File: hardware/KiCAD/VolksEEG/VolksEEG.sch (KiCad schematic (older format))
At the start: 0 parts

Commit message: Added more tasks following re-watch of 1st half of previous design review.
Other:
- note added: "Known Remaining Tasks:\n* Finish Referential Montage configuration of ADS1299 Electrodes.\n* Add Debugging bits, Test points, 0Ohm Links, indicator LEDs? \n* Double Check ADS1299 Connections.\n* Add component values.\n* Adjust names of hierarchical pins to sheets.\n* Seperate Analogue and digital supplies?\n* Check SD Card connections.\n* Decoupling caps.\n* Check Power up sequencing."
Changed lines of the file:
@@
 Title "Main"
 Date ""
-Rev "6378737"
+Rev ""
 Comp "VolksEEG"
 Comment1 ""
@@
 $EndDescr
 $Sheet
-S 6600 3000 1050 2350
+S 6600 1750 1050 2350
 U 615BA110
 F0 "ADS1299" 50
 F1 "ADS1299.sch" 50
-F2 "nCS_ads" I L 6600 3800 50
-F3 "SCK_ads" I L 6600 3950 50
-F4 "MOSI_ads" I L 6600 3500 50
-F5 "MISO_ads" O L 6600 4100 50
-F6 "nRST_ads" I L 6600 3650 50
-F7 "AIN5" I R 7650 4100 50
-F8 "AIN6" I R 7650 4250 50
-F9 "AIN7" I R 7650 4400 50
-F10 "AIN8" I R 7650 4550 50
-F11 "AIN1" I R 7650 3500 50
-F12 "AIN2" I R 7650 3650 50
-F13 "AIN3" I R 7650 3800 50
-F14 "AIN4" I R 7650 3950 50
-F15 "ADS_nDRDY_ads" O L 6600 4250 50
-F16 "+3V3_ads" I L 6600 4500 50
-F17 "+2V5_ads" I L 6600 4650 50
-F18 "-2V5_ads" I L 6600 4800 50
-F19 "GND_ads" I L 6600 4950 50
-F20 "REF" I R 7650 4800 50
-F21 "BIAS_OUT" O R 7650 4950 50
-F22 "BIAS_INV" O R 7650 5100 50
+F2 "nCS_ads" I L 6600 2550 50
+F3 "SCK_ads" I L 6600 2700 50
+F4 "MOSI_ads" I L 6600 2250 50
+F5 "MISO_ads" O L 6600 2850 50
+F6 "nRST_ads" I L 6600 2400 50
+F7 "AIN5" I R 7650 2850 50
+F8 "AIN6" I R 7650 3000 50
+F9 "AIN7" I R 7650 3150 50
+F10 "AIN8" I R 7650 3300 50
+F11 "AIN1" I R 7650 2250 50
+F12 "AIN2" I R 7650 2400 50
+F13 "AIN3" I R 7650 2550 50
+F14 "AIN4" I R 7650 2700 50
+F15 "ADS_nDRDY_ads" O L 6600 3000 50
+F16 "+3V3_ads" I L 6600 3250 50
+F17 "+2V5_ads" I L 6600 3400 50
+F18 "-2V5_ads" I L 6600 3550 50
+F19 "GND_ads" I L 6600 3700 50
+F20 "REF" I R 7650 3550 50
+F21 "BIAS_OUT" O R 7650 3700 50
+F22 "BIAS_INV" O R 7650 3850 50
 $EndSheet
 $Sheet
-S 5250 4350 1000 1000
+S 5250 3100 1000 1000
 U 615BA255
 F0 "ADS1299 Power" 50
 F1 "Power.sch" 50
-F2 "GND_in" I L 5250 4650 50
-F3 "+3V3_out" O R 6250 4500 50
-F4 "+2V5_out" O R 6250 4650 50
-F5 "-2V5_out" O R 6250 4800 50
-F6 "+5V_in" I L 5250 4500 50
+F2 "GND_in" I L 5250 3400 50
+F3 "+3V3_out" O R 6250 3250 50
+F4 "+2V5_out" O R 6250 3400 50
+F5 "-2V5_out" O R 6250 3550 50
+F6 "+5V_in" I L 5250 3250 50
 $EndSheet
 $Sheet
-S 1500 3200 1200 1400
+S 1500 1950 1200 1400
 U 615BA20B
 F0 "nRF52840 Feather Sense Express Board" 50
 F1 "nRF52840.sch" 50
-F2 "MOSI_nrf" O R 2700 3500 50
-F3 "SCK_nrf" O R 2700 3950 50
-F4 "MISO_nrf" I R 2700 4100 50
-F5 "ADS-nRST_nrf" O R 2700 3650 50
-F6 "ADS-nCS_nrf" O R 2700 3800 50
-F7 "ADS-nDRDY_nrf" I R 2700 4250 50
-F8 "+3V3_nrf" O R 2700 3350 50
-F9 "GND_nrf" O R 2700 4400 50
+F2 "MOSI_nrf" O R 2700 2250 50
+F3 "SCK_nrf" O R 2700 2700 50
+F4 "MISO_nrf" I R 2700 2850 50
+F5 "ADS-nRST_nrf" O R 2700 2400 50
+F6 "ADS-nCS_nrf" O R 2700 2550 50
+F7 "ADS-nDRDY_nrf" I R 2700 3000 50
+F8 "+3V3_nrf" O R 2700 2100 50
+F9 "GND_nrf" O R 2700 3150 50
 $EndSheet
 Wire Wire Line
-	2700 3500 3450 3500
+	2700 2250 3450 2250
 Wire Wire Line
-	3450 3650 2700 3650
+	3450 2400 2700 2400
 Wire Wire Line
-	2700 3800 3450 3800
+	2700 2550 3450 2550
 Wire Wire Line
-	3450 3950 2700 3950
+	3450 2700 2700 2700
 Wire Wire Line
-	2700 4100 3450 4100
+	2700 2850 3450 2850
 Wire Wire Line
-	8150 4100 7650 4100
+	8150 2850 7650 2850
 Wire Wire Line
-	4800 3500 6600 3500
+	4800 2250 6600 2250
 Wire Wire Line
-	4800 3650 6600 3650
+	4800 2400 6600 2400
 Wire Wire Line
-	4800 3800 6600 3800
+	4800 2550 6600 2550
 Wire Wire Line
-	4800 3950 6600 3950
+	4800 2700 6600 2700
 Wire Wire Line
-	4800 4100 6600 4100
+	4800 2850 6600 2850
 Wire Wire Line
-	6600 4250 4800 4250
+	6600 3000 4800 3000
 Wire Wire Line
-	4800 4550 4950 4550
+	4800 3300 4950 3300
 Wire Wire Line
-	4950 4550 4950 4650
+	4950 3300 4950 3400
 Wire Wire Line
-	4950 4650 5250 4650
+	4950 3400 5250 3400
 Wire Wire Line
-	6250 4500 6400 4500
+	6250 3250 6400 3250
 Wire Wire Line
-	6600 4650 6250 4650
+	6600 3400 6250 3400
 Wire Wire Line
-	6250 4800 6600 4800
+	6250 3550 6600 3550
 Wire Wire Line
-	2700 4250 3450 4250
+	2700 3000 3450 3000
 Wire Wire Line
-	2700 3350 3450 3350
+	2700 2100 3450 2100
 Wire Wire Line
-	2700 4400 3450 4400
+	2700 3150 3450 3150
 $Sheet
-S 3450 3250 1350 1400
+S 3450 2000 1350 1400
 U 61731DC5
 F0 "Isolation" 50
 F1 "isolation.sch" 50
-F2 "+3V3_ni" I L 3450 3350 50
-F3 "GND_ni" I L 3450 4400 50
-F4 "+3V3_iso" I R 4800 3350 50
-F5 "GND_iso" O R 4800 4550 50
-F6 "MOSI_iso" O R 4800 3500 50
-F7 "ADS_nRST_iso" O R 4800 3650 50
-F8 "nCS_iso" O R 4800 3800 50
-F9 "SCK_iso" O R 4800 3950 50
-F10 "MISO_iso" I R 4800 4100 50
-F11 "ADS_nDRDY_iso" I R 4800 4250 50
-F12 "MOSI_ni" I L 3450 3500 50
-F13 "ADS_nRST_ni" I L 3450 3650 50
-F14 "nCS_ni" I L 3450 3800 50
-F15 "SCK_ni" I L 3450 3950 50
-F16 "MISO_ni" O L 3450 4100 50
-F17 "ADS_nDRDY_ni" O L 3450 4250 50
-F18 "+5V_iso" O R 4800 4400 50
+F2 "+3V3_ni" I L 3450 2100 50
+F3 "GND_ni" I L 3450 3150 50
+F4 "+3V3_iso" I R 4800 2100 50
+F5 "GND_iso" O R 4800 3300 50
+F6 "MOSI_iso" O R 4800 2250 50
+F7 "ADS_nRST_iso" O R 4800 2400 50
+F8 "nCS_iso" O R 4800 2550 50
+F9 "SCK_iso" O R 4800 2700 50
+F10 "MISO_iso" I R 4800 2850 50
+F11 "ADS_nDRDY_iso" I R 4800 3000 50
+F12 "MOSI_ni" I L 3450 2250 50
+F13 "ADS_nRST_ni" I L 3450 2400 50
+F14 "nCS_ni" I L 3450 2550 50
+F15 "SCK_ni" I L 3450 2700 50
+F16 "MISO_ni" O L 3450 2850 50
+F17 "ADS_nDRDY_ni" O L 3450 3000 50
+F18 "+5V_iso" O R 4800 3150 50
 $EndSheet
 Wire Wire Line
-	4800 4400 5050 4400
+	4800 3150 5050 3150
 Wire Wire Line
-	6400 3350 6400 4500
+	6400 2100 6400 3250
 Wire Wire Line
-	4800 3350 6400 3350
-Connection ~ 6400 4500
+	4800 2100 6400 2100
+Connection ~ 6400 3250
 Wire Wire Line
-	6400 4500 6600 4500
+	6400 3250 6600 3250
 Wire Wire Line
-	5050 4400 5050 4500
+	5050 3150 5050 3250
 Wire Wire Line
-	5050 4500 5250 4500
+	5050 3250 5250 3250
 Wire Wire Line
-	6600 4950 6400 4950
+	6600 3700 6400 3700
 Wire Wire Line
-	6400 4950 6400 5500
+	6400 3700 6400 4250
 Wire Wire Line
-	6400 5500 4950 5500
+	6400 4250 4950 4250
 Wire Wire Line
-	4950 5500 4950 4650
-Connection ~ 4950 4650
+	4950 4250 4950 3400
+Connection ~ 4950 3400
 $Sheet
-S 8150 3000 800  2350
+S 8150 1750 800  2350
 U 615BA18D
 F0 "EEG Electrodes" 50
 F1 "EEG-Electrodes.sch" 50
-F2 "AIN2" O L 8150 3650 50
-F3 "AIN1" O L 8150 3500 50
-F4 "AIN3" O L 8150 3800 50
-F5 "AIN4" O L 8150 3950 50
-F6 "AIN5" O L 8150 4100 50
-F7 "AIN6" O L 8150 4250 50
-F8 "AIN7" O L 8150 4400 50
-F9 "AIN8" O L 8150 4550 50
-F10 "REF" O L 8150 4800 50
-F11 "BIAS_OUT" I L 8150 4950 50
-F12 "BIAS_INV" I L 8150 5100 50
+F2 "AIN2" O L 8150 2400 50
+F3 "AIN1" O L 8150 2250 50
+F4 "AIN3" O L 8150 2550 50
+F5 "AIN4" O L 8150 2700 50
+F6 "AIN5" O L 8150 2850 50
+F7 "AIN6" O L 8150 3000 50
+F8 "AIN7" O L 8150 3150 50
+F9 "AIN8" O L 8150 3300 50
+F10 "REF" O L 8150 3550 50
+F11 "BIAS_OUT" I L 8150 3700 50
+F12 "BIAS_INV" I L 8150 3850 50
 $EndSheet
 Wire Wire Line
-	7650 3500 8150 3500
+	7650 2250 8150 2250
 Wire Wire Line
-	8150 3650 7650 3650
+	8150 2400 7650 2400
 Wire Wire Line
-	7650 3800 8150 3800
+	7650 2550 8150 2550
 Wire Wire Line
-	8150 3950 7650 3950
+	8150 2700 7650 2700
 Wire Wire Line
-	7650 4250 8150 4250
+	7650 3000 8150 3000
 Wire Wire Line
-	8150 4400 7650 4400
+	8150 3150 7650 3150
 Wire Wire Line
-	7650 4550 8150 4550
+	7650 3300 8150 3300
 Wire Wire Line
-	7650 4800 8150 4800
+	7650 3550 8150 3550
 Wire Wire Line
-	8150 4950 7650 4950
+	8150 3700 7650 3700
 Wire Wire Line
-	7650 5100 8150 5100
+	7650 3850 8150 3850
+Text Notes 1550 5550 0    50   ~ 0
+Known Remaining Tasks:\n* Finish Referential Montage configuration of ADS1299 Electrodes.\n* Add Debugging bits, Test points, 0Ohm Links, indicator LEDs? \n* Double Check ADS1299 Connections.\n* Add component values.\n* Adjust names of hierarchical pins to sheets.\n* Seperate Analogue and digital supplies?\n* Check SD Card connections.\n* Decoupling caps.\n* Check Power up sequencing.
 $EndSCHEMATC

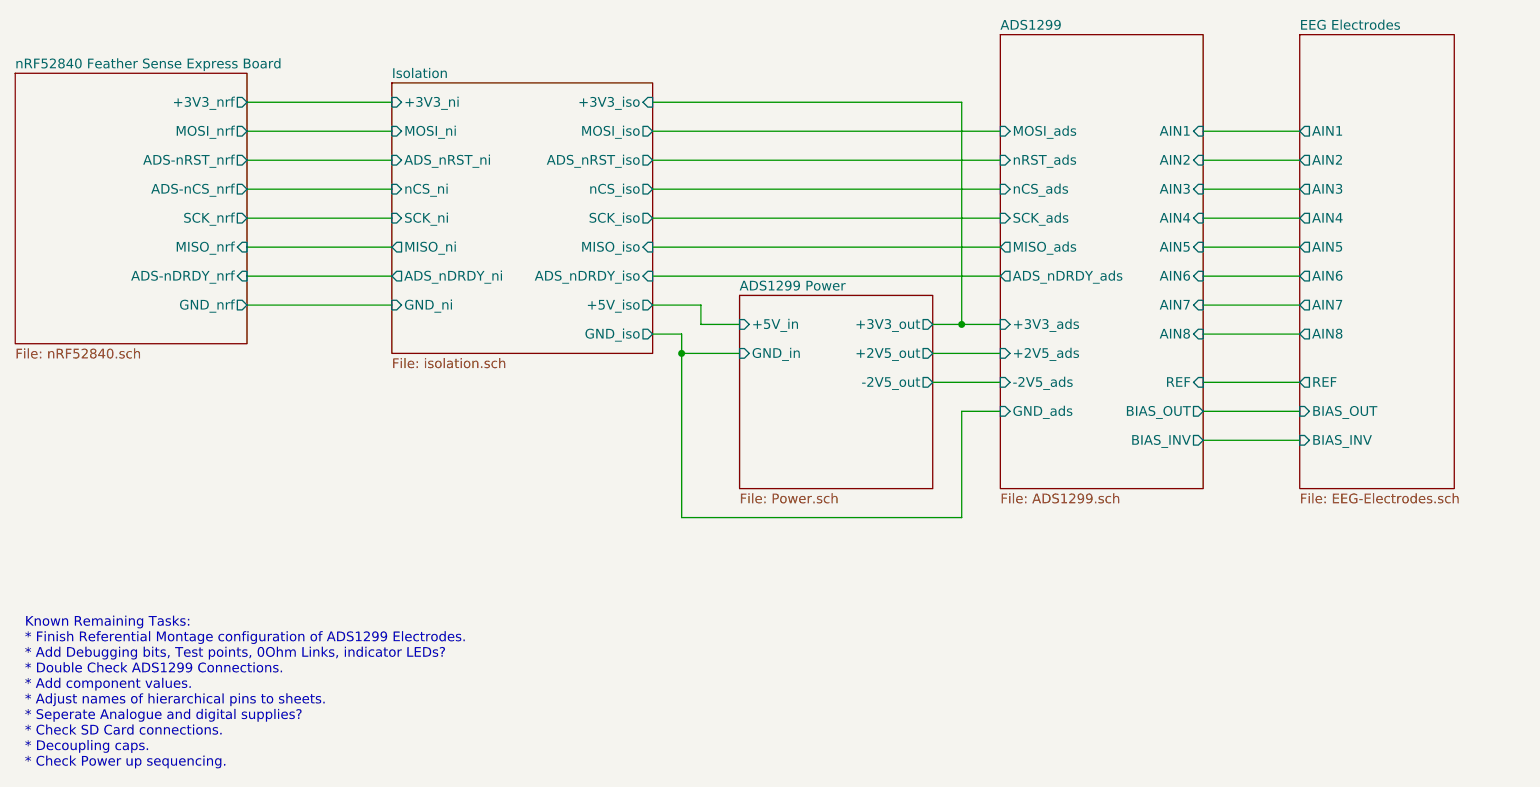
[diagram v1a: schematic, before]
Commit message: Updated names of heirarchical pins, finished referential montage configuration, added filter cap to ADS_nRST line, started putting ADS1299 gpios to a header.
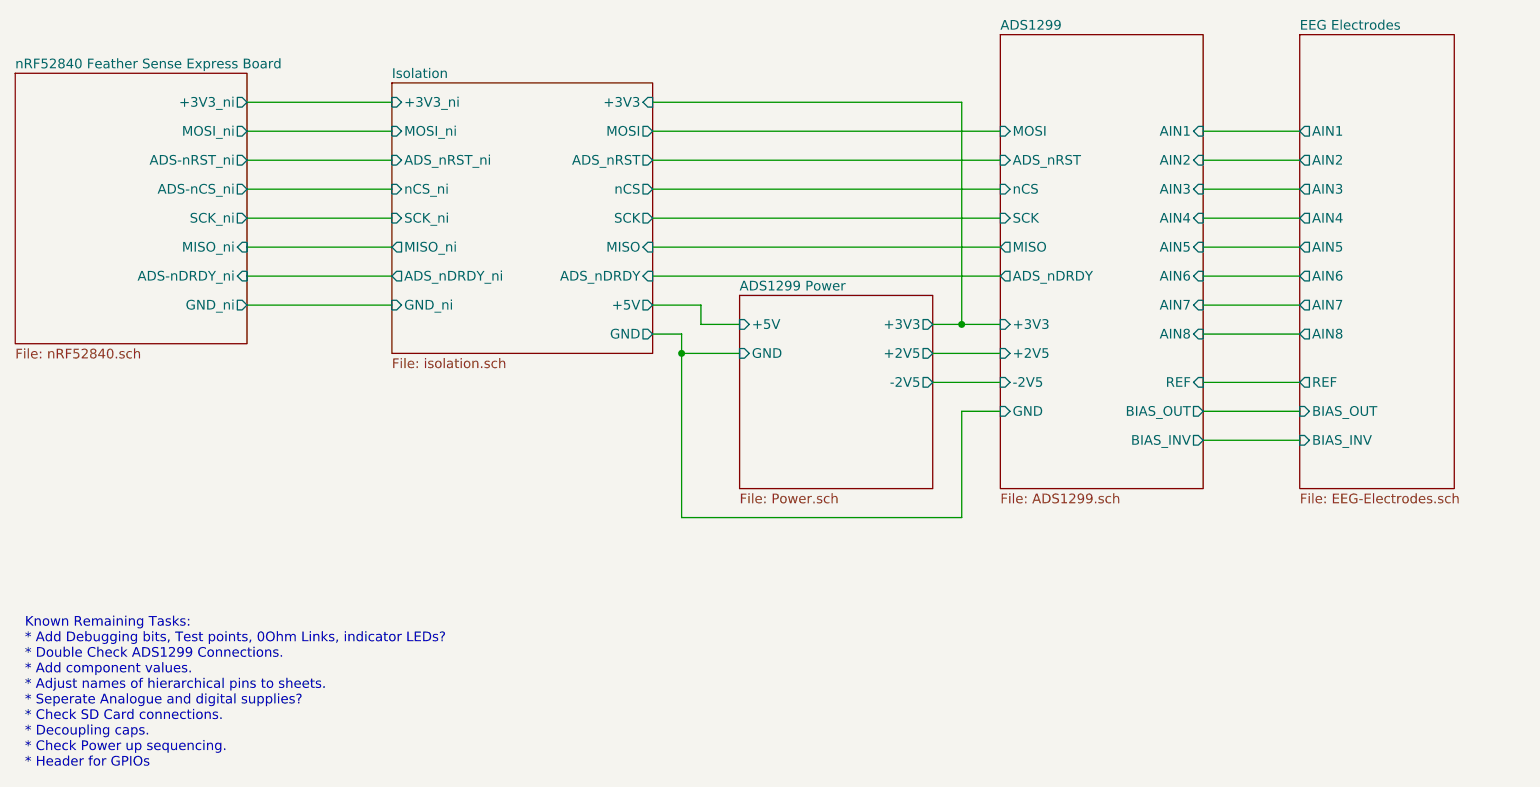
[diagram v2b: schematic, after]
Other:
- note added: "Known Remaining Tasks:\n* Add Debugging bits, Test points, 0Ohm Links, indicator LEDs? \n* Double Check ADS1299 Connections.\n* Add component values.\n* Adjust names of hierarchical pins to sheets.\n* Seperate Analogue and digital supplies?\n* Check SD Card connections.\n* Decoupling caps.\n* Check Power up sequencing.\n* Header for GPIOs"
- note removed: "Known Remaining Tasks:\n* Finish Referential Montage configuration of ADS1299 Electrodes.\n* Add Debugging bits, Test points, 0Ohm Links, indicator LEDs? \n* Double Check ADS1299 Connections.\n* Add component values.\n* Adjust names of hierarchical pins to sheets.\n* Seperate Analogue and digital supplies?\n* Check SD Card connections.\n* Decoupling caps.\n* Check Power up sequencing."
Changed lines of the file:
@@
 F0 "ADS1299" 50
 F1 "ADS1299.sch" 50
-F2 "nCS_ads" I L 6600 2550 50
-F3 "SCK_ads" I L 6600 2700 50
-F4 "MOSI_ads" I L 6600 2250 50
-F5 "MISO_ads" O L 6600 2850 50
-F6 "nRST_ads" I L 6600 2400 50
+F2 "nCS" I L 6600 2550 50
+F3 "SCK" I L 6600 2700 50
+F4 "MOSI" I L 6600 2250 50
+F5 "MISO" O L 6600 2850 50
+F6 "ADS_nRST" I L 6600 2400 50
 F7 "AIN5" I R 7650 2850 50
 F8 "AIN6" I R 7650 3000 50
@@
 F13 "AIN3" I R 7650 2550 50
 F14 "AIN4" I R 7650 2700 50
-F15 "ADS_nDRDY_ads" O L 6600 3000 50
-F16 "+3V3_ads" I L 6600 3250 50
-F17 "+2V5_ads" I L 6600 3400 50
-F18 "-2V5_ads" I L 6600 3550 50
-F19 "GND_ads" I L 6600 3700 50
+F15 "ADS_nDRDY" O L 6600 3000 50
+F16 "+3V3" I L 6600 3250 50
+F17 "+2V5" I L 6600 3400 50
+F18 "-2V5" I L 6600 3550 50
+F19 "GND" I L 6600 3700 50
 F20 "REF" I R 7650 3550 50
 F21 "BIAS_OUT" O R 7650 3700 50
@@
 F0 "ADS1299 Power" 50
 F1 "Power.sch" 50
-F2 "GND_in" I L 5250 3400 50
-F3 "+3V3_out" O R 6250 3250 50
-F4 "+2V5_out" O R 6250 3400 50
-F5 "-2V5_out" O R 6250 3550 50
-F6 "+5V_in" I L 5250 3250 50
+F2 "GND" I L 5250 3400 50
+F3 "+3V3" O R 6250 3250 50
+F4 "+2V5" O R 6250 3400 50
+F5 "-2V5" O R 6250 3550 50
+F6 "+5V" I L 5250 3250 50
 $EndSheet
 $Sheet
@@
 F0 "nRF52840 Feather Sense Express Board" 50
 F1 "nRF52840.sch" 50
-F2 "MOSI_nrf" O R 2700 2250 50
-F3 "SCK_nrf" O R 2700 2700 50
-F4 "MISO_nrf" I R 2700 2850 50
-F5 "ADS-nRST_nrf" O R 2700 2400 50
-F6 "ADS-nCS_nrf" O R 2700 2550 50
-F7 "ADS-nDRDY_nrf" I R 2700 3000 50
-F8 "+3V3_nrf" O R 2700 2100 50
-F9 "GND_nrf" O R 2700 3150 50
+F2 "MOSI_ni" O R 2700 2250 50
+F3 "SCK_ni" O R 2700 2700 50
+F4 "MISO_ni" I R 2700 2850 50
+F5 "ADS-nRST_ni" O R 2700 2400 50
+F6 "ADS-nCS_ni" O R 2700 2550 50
+F7 "ADS-nDRDY_ni" I R 2700 3000 50
+F8 "+3V3_ni" O R 2700 2100 50
+F9 "GND_ni" O R 2700 3150 50
 $EndSheet
 Wire Wire Line
@@
 F2 "+3V3_ni" I L 3450 2100 50
 F3 "GND_ni" I L 3450 3150 50
-F4 "+3V3_iso" I R 4800 2100 50
-F5 "GND_iso" O R 4800 3300 50
-F6 "MOSI_iso" O R 4800 2250 50
-F7 "ADS_nRST_iso" O R 4800 2400 50
-F8 "nCS_iso" O R 4800 2550 50
-F9 "SCK_iso" O R 4800 2700 50
-F10 "MISO_iso" I R 4800 2850 50
-F11 "ADS_nDRDY_iso" I R 4800 3000 50
+F4 "+3V3" I R 4800 2100 50
+F5 "GND" O R 4800 3300 50
+F6 "MOSI" O R 4800 2250 50
+F7 "ADS_nRST" O R 4800 2400 50
+F8 "nCS" O R 4800 2550 50
+F9 "SCK" O R 4800 2700 50
+F10 "MISO" I R 4800 2850 50
+F11 "ADS_nDRDY" I R 4800 3000 50
 F12 "MOSI_ni" I L 3450 2250 50
 F13 "ADS_nRST_ni" I L 3450 2400 50
@@
 F16 "MISO_ni" O L 3450 2850 50
 F17 "ADS_nDRDY_ni" O L 3450 3000 50
-F18 "+5V_iso" O R 4800 3150 50
+F18 "+5V" O R 4800 3150 50
 $EndSheet
 Wire Wire Line
@@
 	7650 3850 8150 3850
 Text Notes 1550 5550 0    50   ~ 0
-Known Remaining Tasks:\n* Finish Referential Montage configuration of ADS1299 Electrodes.\n* Add Debugging bits, Test points, 0Ohm Links, indicator LEDs? \n* Double Check ADS1299 Connections.\n* Add component values.\n* Adjust names of hierarchical pins to sheets.\n* Seperate Analogue and digital supplies?\n* Check SD Card connections.\n* Decoupling caps.\n* Check Power up sequencing.
+Known Remaining Tasks:\n* Add Debugging bits, Test points, 0Ohm Links, indicator LEDs? \n* Double Check ADS1299 Connections.\n* Add component values.\n* Adjust names of hierarchical pins to sheets.\n* Seperate Analogue and digital supplies?\n* Check SD Card connections.\n* Decoupling caps.\n* Check Power up sequencing.\n* Header for GPIOs
 $EndSCHEMATC

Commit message: Added custom power symbols for non isolated power. Seperated Analogue and digital supplies. finished putting the ADS1299 GPIOs to a header.
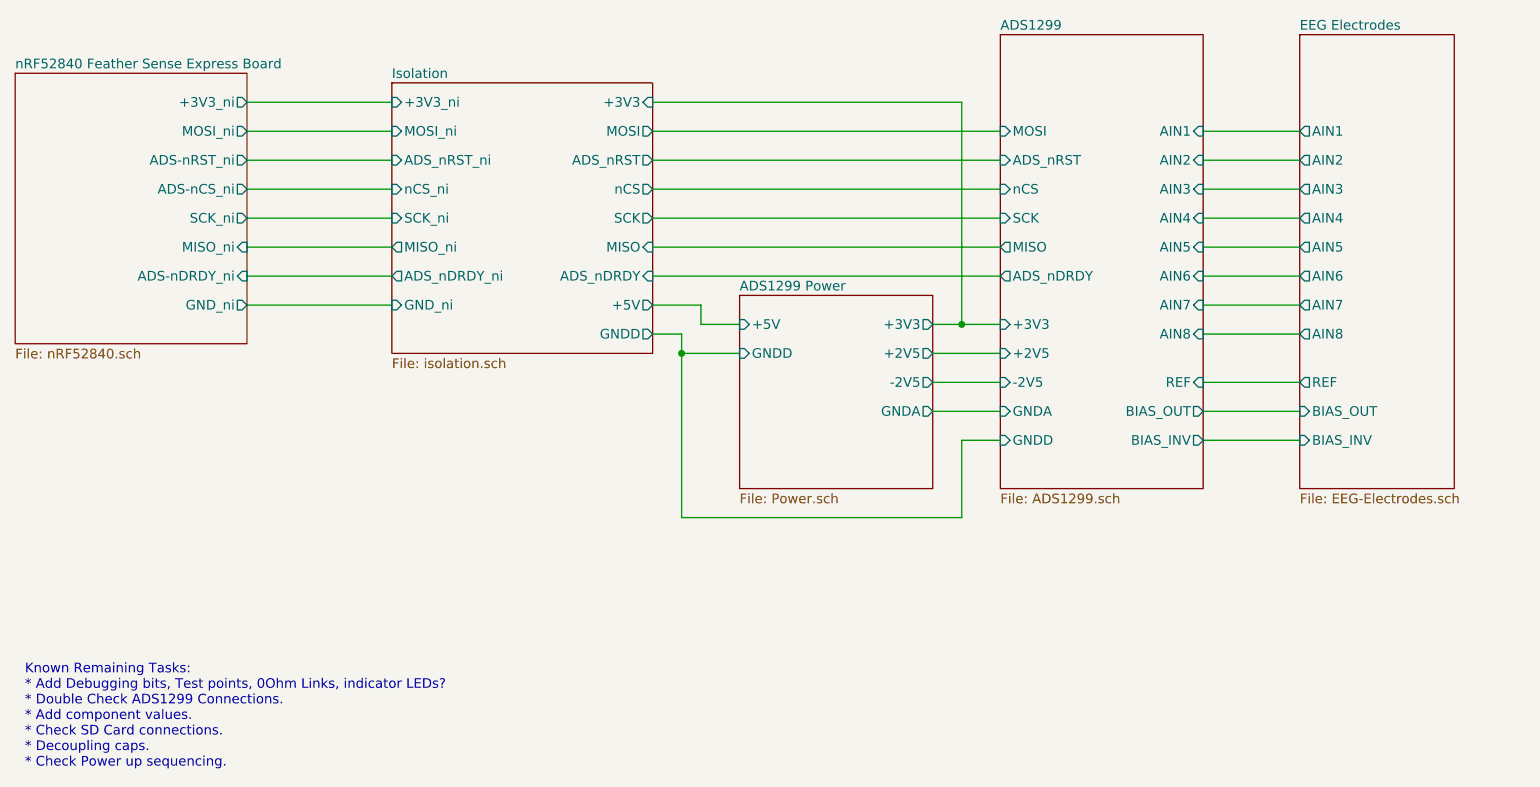
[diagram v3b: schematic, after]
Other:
- note added: "Known Remaining Tasks:\n* Add Debugging bits, Test points, 0Ohm Links, indicator LEDs? \n* Double Check ADS1299 Connections.\n* Add component values.\n* Check SD Card connections.\n* Decoupling caps.\n* Check Power up sequencing."
- note removed: "Known Remaining Tasks:\n* Add Debugging bits, Test points, 0Ohm Links, indicator LEDs? \n* Double Check ADS1299 Connections.\n* Add component values.\n* Adjust names of hierarchical pins to sheets.\n* Seperate Analogue and digital supplies?\n* Check SD Card connections.\n* Decoupling caps.\n* Check Power up sequencing.\n* Header for GPIOs"
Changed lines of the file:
@@
 F17 "+2V5" I L 6600 3400 50
 F18 "-2V5" I L 6600 3550 50
-F19 "GND" I L 6600 3700 50
+F19 "GNDD" I L 6600 3850 50
 F20 "REF" I R 7650 3550 50
 F21 "BIAS_OUT" O R 7650 3700 50
 F22 "BIAS_INV" O R 7650 3850 50
+F23 "GNDA" I L 6600 3700 50
 $EndSheet
 $Sheet
@@
 F0 "ADS1299 Power" 50
 F1 "Power.sch" 50
-F2 "GND" I L 5250 3400 50
+F2 "GNDD" I L 5250 3400 50
 F3 "+3V3" O R 6250 3250 50
 F4 "+2V5" O R 6250 3400 50
 F5 "-2V5" O R 6250 3550 50
 F6 "+5V" I L 5250 3250 50
+F7 "GNDA" O R 6250 3700 50
 $EndSheet
 $Sheet
@@
 F3 "GND_ni" I L 3450 3150 50
 F4 "+3V3" I R 4800 2100 50
-F5 "GND" O R 4800 3300 50
+F5 "GNDD" O R 4800 3300 50
 F6 "MOSI" O R 4800 2250 50
 F7 "ADS_nRST" O R 4800 2400 50
@@
 	5050 3250 5250 3250
 Wire Wire Line
-	6600 3700 6400 3700
+	6600 3850 6400 3850
 Wire Wire Line
-	6400 3700 6400 4250
+	6400 3850 6400 4250
 Wire Wire Line
 	6400 4250 4950 4250
@@
 	7650 3850 8150 3850
 Text Notes 1550 5550 0    50   ~ 0
-Known Remaining Tasks:\n* Add Debugging bits, Test points, 0Ohm Links, indicator LEDs? \n* Double Check ADS1299 Connections.\n* Add component values.\n* Adjust names of hierarchical pins to sheets.\n* Seperate Analogue and digital supplies?\n* Check SD Card connections.\n* Decoupling caps.\n* Check Power up sequencing.\n* Header for GPIOs
+Known Remaining Tasks:\n* Add Debugging bits, Test points, 0Ohm Links, indicator LEDs? \n* Double Check ADS1299 Connections.\n* Add component values.\n* Check SD Card connections.\n* Decoupling caps.\n* Check Power up sequencing.
+Wire Wire Line
+	6250 3700 6600 3700
 $EndSCHEMATC
